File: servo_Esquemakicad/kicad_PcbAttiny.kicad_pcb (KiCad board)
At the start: 2 copper layers, 56 parts, among them J1 Conn_02x01, J10 Conn_01x04, J11 Conn_01x04, J12 Conn_01x04, J13 Conn_01x04, J2 Conn_02x02_Odd_Even, J3 Conn_02x02_Odd_Even, J4 Conn_01x04, J5 ESP01, J6 Conn_01x04, J7 Conn_01x04, J8 Conn_01x04, J9 Conn_01x04, K1 SANYOU_SRD_Form_C, K2 SANYOU_SRD_Form_C, K3 SANYOU_SRD_Form_C, K4 SANYOU_SRD_Form_C, K5 SANYOU_SRD_Form_C, K6 SANYOU_SRD_Form_C, K7 SANYOU_SRD_Form_C, K8 SANYOU_SRD_Form_C, Q1 2N2219, Q2 2N2219, Q3 2N2219, Q4 2N2219, Q5 2N2219, Q6 2N2219, Q7 2N2219, Q8 2N2219, U1 ATtiny85V-10PU, U2 74HC595, U3 L7809, U4 L7805, U5 LM317

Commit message: att
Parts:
- removed the C1 at (123.6, 56.5)
- removed C3: 220u, Capacitor_THT:CP_Radial_D5.0mm_P2.50mm
- removed J1: Conn_02x01, Connector_PinHeader_2.54mm:PinHeader_2x01_P2.54mm_Vertical
- removed the J2 at (127.6, 47.5)
- removed the J3 at (176.3, 47.5)
- removed the U3 at (140.6, 49.0)
- removed U4: L7805, Package_TO_SOT_THT:TO-220-3_Vertical
- C1: renamed from C4; value 47u -> 0.1u
- C2: value 47u -> 10u
- J2: renamed from J4; value Conn_01x04 -> RF
- moved R1 60.9 mm to (148.6, 53.3), turned to 180 degrees
- moved U2 55.3 mm to (138.4, 58.4), turned to 270 degrees
- moved U1 48.8 mm to (153.7, 114.3), turned to 90 degrees
- moved R8 41.4 mm to (118.1, 121.9), turned to 90 degrees
- moved R2 39.9 mm to (141.0, 69.8)
- moved C1 37.5 mm to (132.1, 57.1)
- moved U3 35.7 mm to (129.5, 114.3)
- moved R7 28.4 mm to (118.1, 100.3), turned to 90 degrees
- moved R9 20.6 mm to (171.4, 121.9), turned to 90 degrees
- moved R6 18.7 mm to (118.1, 80.0), turned to 90 degrees
- moved J3 16.1 mm to (141.0, 78.7)
- moved R5 16.0 mm to (118.1, 58.4), turned to 90 degrees
- moved J2 13.6 mm to (151.1, 76.2)
- moved C2 11.0 mm to (133.3, 67.3), turned to 90 degrees
- moved R12 8.34 mm to (171.4, 59.7), turned to 90 degrees
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- renumbered D5 to D1, D1 to D2, D6 to D3, D2 to D4, D7 to D5, D3 to D6, D8 to D7, D4 to D8, J13 to J10, J6 to J11, J5 to J3, J10 to J4, J9 to J5, J11 to J6, J8 to J7, J12 to J8, J7 to J9, K5 to K1, K1 to K2, K6 to K3, K2 to K4, K7 to K5, K3 to K6, K8 to K7, K4 to K8, Q5 to Q2, Q2 to Q3, Q6 to Q4, Q3 to Q5, Q7 to Q6, Q4 to Q7, R9 to R1, R3 to R10, R2 to R11, R1 to R12, R10 to R2, R8 to R5, R7 to R6, R6 to R7, R5 to R8, R4 to R9, U5 to U2, U2 to U3
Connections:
- C1 pad 2: GND -> Net-(C1-Pad2)
- C2 pad 1: Net-(C2-Pad1) -> /+3.3V
- C2 pad 2: GND -> Net-(C1-Pad2)
- J10 pad 3: Net-(J13-Pad3) -> (no net)
- J11 pad 3: Net-(J6-Pad3) -> (no net)
- J3 pad 3: Net-(J5-Pad3) -> (no net)
- J3 pad 5: Net-(J5-Pad5) -> (no net)
- J3 pad 6: Net-(J5-Pad6) -> (no net)
- J4 pad 3: Net-(J10-Pad3) -> (no net)
- J5 pad 3: Net-(J9-Pad3) -> (no net)
- J6 pad 3: Net-(J11-Pad3) -> (no net)
- J7 pad 3: Net-(J8-Pad3) -> (no net)
- J8 pad 3: Net-(J12-Pad3) -> (no net)
- J9 pad 3: Net-(J7-Pad3) -> (no net)
- Q1 pad 3: Net-(J3-Pad1) -> /+5V
- Q2 pad 3: Net-(J3-Pad1) -> /+5V
- Q3 pad 3: Net-(J3-Pad1) -> /+5V
- Q4 pad 3: Net-(J3-Pad1) -> /+5V
- Q5 pad 3: Net-(J3-Pad1) -> /+5V
- Q6 pad 3: Net-(J3-Pad1) -> /+5V
- Q7 pad 3: Net-(J3-Pad1) -> /+5V
- Q8 pad 3: Net-(J3-Pad1) -> /+5V
- R1 pad 2: GND -> Net-(C1-Pad2)
- U1 pad 8: Net-(U1-Pad8) -> (no net)
- U3 pad 9: Net-(U2-Pad9) -> (no net)
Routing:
- net GND: track 637.4 -> 255.0 mm
- net Net-(J3-Pad1): track 295.8 -> 0.00 mm, vias 6 -> 0
- net /RX: track 117.4 -> 0.00 mm, vias 4 -> 0
- net /+3.3V: track 84.6 -> 0.00 mm
- net Net-(C1-Pad1): track 82.6 -> 0.00 mm, vias 8 -> 0
- net +12V: track 74.8 -> 0.00 mm, vias 4 -> 0
- net /TX: track 69.6 -> 0.00 mm
- net /EN: track 59.4 -> 0.00 mm, vias 4 -> 0
- net /Q4: track 41.3 -> 0.00 mm
- net Net-(C1-Pad1) (its old number): track 40.9 -> 0.00 mm
- net Net-(C2-Pad1): track 38.6 -> 0.00 mm
- net Net-(R11-Pad1): track 35.1 -> 0.00 mm
- net Net-(R12-Pad1): track 30.4 -> 0.00 mm
- net Net-(R9-Pad1): track 30.0 -> 0.00 mm
- net /Q3: track 26.8 -> 0.00 mm
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- removed copper zone on B.Cu, net (none)
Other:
- board text removed: "+12V"
- board text removed: "+5V"
- board text removed: "7805"
- board text removed: "7809"
- board text removed: "Alim"
- board text removed: "Alim."
- board text removed: "GND"
- board text removed: "J4"
- board text removed: "J5"
- board text removed: "Jumper"

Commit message: retirada de componentes desnecessarios
após analise vi q vários componentes n tinham razão pra existir então foram retirado
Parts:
- removed D1, D2, D3, D4, D5, D6, D7, D8: 1N4007, Diode_THT:D_DO-41_SOD81_P10.16mm_Horizontal
- removed J10, J11, J4, J5, J6, J7, J8, J9: Conn_01x04, TerminalBlock:TerminalBlock_bornier-4_P5.08mm
- removed K1, K2, K3, K4, K5, K6, K7, K8: SANYOU_SRD_Form_C, Relay_THT:Relay_SPDT_SANYOU_SRD_Series_Form_C
- removed U1: ATtiny85V-10PU, Package_DIP:DIP-8_W7.62mm_Socket
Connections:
- Q1 pad 1: /K1 -> (no net)
- Q1 pad 3: /+5V -> (no net)
- Q2 pad 1: /K5 -> (no net)
- Q2 pad 3: /+5V -> (no net)
- Q3 pad 1: /K2 -> (no net)
- Q3 pad 3: /+5V -> (no net)
- Q4 pad 1: /K6 -> (no net)
- Q4 pad 3: /+5V -> (no net)
- Q5 pad 1: /K3 -> (no net)
- Q5 pad 3: /+5V -> (no net)
- Q6 pad 1: /K7 -> (no net)
- Q6 pad 3: /+5V -> (no net)
- Q7 pad 1: /K4 -> (no net)
- Q7 pad 3: /+5V -> (no net)
- Q8 pad 1: /K8 -> (no net)
- Q8 pad 3: /+5V -> (no net)
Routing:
- net GND: track 255.0 -> 0.00 mm
- net /+5V: track 78.0 -> 0.00 mm, vias 6 -> 0
- net Net-(J8-Pad4): track 29.2 -> 0.00 mm
- net Net-(J6-Pad4): track 29.2 -> 0.00 mm
- net Net-(J4-Pad4): track 29.2 -> 0.00 mm
- net Net-(J10-Pad4): track 29.2 -> 0.00 mm
- net Net-(J9-Pad4): track 28.3 -> 0.00 mm
- net Net-(J7-Pad4): track 28.3 -> 0.00 mm
- net Net-(J11-Pad4): track 28.3 -> 0.00 mm
- net Net-(J5-Pad4): track 28.3 -> 0.00 mm
- net /K7: track 19.1 -> 0.00 mm
- net /K6: track 19.1 -> 0.00 mm
- net /K5: track 19.1 -> 0.00 mm
- net /K8: track 19.1 -> 0.00 mm
- net /K4: track 19.0 -> 0.00 mm
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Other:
- board text removed: "COM"
- board text removed: "NC"
- board text removed: "NF"
- board text removed: "NO"

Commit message: atualizações do esquematico e design PCB
Atualizada o esquemático com as novas conexões p/ os transistores
Atualizado o designe PCB com os novos footprints
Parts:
- removed C1: 0.1u, Capacitor_THT:CP_Radial_D5.0mm_P2.50mm
- removed C2: 10u, Capacitor_THT:CP_Radial_D5.0mm_P2.50mm
- removed R1: 220R, Resistor_THT:R_Axial_DIN0207_L6.3mm_D2.5mm_P10.16mm_Horizontal
- removed R2: 360R, Resistor_THT:R_Axial_DIN0207_L6.3mm_D2.5mm_P10.16mm_Horizontal
- removed U2: LM317, Package_TO_SOT_THT:TO-220-3_Horizontal_TabDown
- added J1: Jack-DC, Connector_BarrelJack:BarrelJack_Horizontal, F.Cu at (226.3, 50.6)
- added R3: 2k, Resistor_THT:R_Axial_DIN0207_L6.3mm_D2.5mm_P10.16mm_Horizontal, F.Cu at (213.3, 59.9)
- added R4: 1k, Resistor_THT:R_Axial_DIN0207_L6.3mm_D2.5mm_P10.16mm_Horizontal, F.Cu at (230.4, 47.2)
- added U1: ATtiny85, Package_SO:SOIJ-8_5.3x5.3mm_P1.27mm, F.Cu at (197.5, 50.2)

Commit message: init design PCB
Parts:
- removed U1: ATtiny85, Package_SO:SOIJ-8_5.3x5.3mm_P1.27mm
- added U2: ATtiny85-20PU, Package_DIP:DIP-8_W7.62mm, F.Cu at (167.6, 57.1)
- moved J1 111.6 mm to (115.6, 64.8), turned to 270 degrees
- moved R4 94.6 mm to (135.9, 52.1), turned to 180 degrees
- moved R3 60.2 mm to (153.7, 52.1), turned to 180 degrees
- moved R8 53.2 mm to (141.4, 74.0), turned to 270 degrees
- moved R9 51.9 mm to (151.4, 74.0), turned to 270 degrees
- moved U3 49.8 mm to (124.5, 64.8)
- moved Q7 42.4 mm to (142.7, 89.0), turned to 180 degrees
- moved J3 40.6 mm to (179.1, 64.8), turned to 180 degrees
- moved Q8 37.1 mm to (182.7, 89.0), turned to 180 degrees
- moved Q2 36.6 mm to (152.7, 89.0), turned to 180 degrees
- moved Q1 34.2 mm to (112.7, 89.0), turned to 180 degrees
- moved R7 29.5 mm to (131.4, 74.0), turned to 270 degrees
- moved R10 29.3 mm to (161.4, 74.0), turned to 270 degrees
- moved J2 27.3 mm to (163.8, 52.1)
- moved Q5 22.5 mm to (132.7, 89.0), turned to 180 degrees
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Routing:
- net /+5V: track 0.00 -> 115.5 mm
- net /TX: track 0.00 -> 69.9 mm
- net Net-(R12-Pad1): track 0.00 -> 46.3 mm
- net Net-(R11-Pad1): track 0.00 -> 41.3 mm
- net Net-(U2-Pad6): track 0.00 -> 39.0 mm
- net Net-(U2-Pad7): track 0.00 -> 34.7 mm
- net Net-(R10-Pad1): track 0.00 -> 33.8 mm
- net GND: track 0.00 -> 30.0 mm
- net Net-(R5-Pad1): track 0.00 -> 29.3 mm
- net Net-(R9-Pad1): track 0.00 -> 26.2 mm
- net Net-(U2-Pad5): track 0.00 -> 26.0 mm
- net Net-(R8-Pad1): track 0.00 -> 19.4 mm
- net /RX: track 0.00 -> 13.0 mm
- net Net-(R6-Pad1): track 0.00 -> 11.3 mm
- net Net-(R7-Pad1): track 0.00 -> 10.9 mm
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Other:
- board text removed: "ATtiny85"
- board text removed: "LM317"

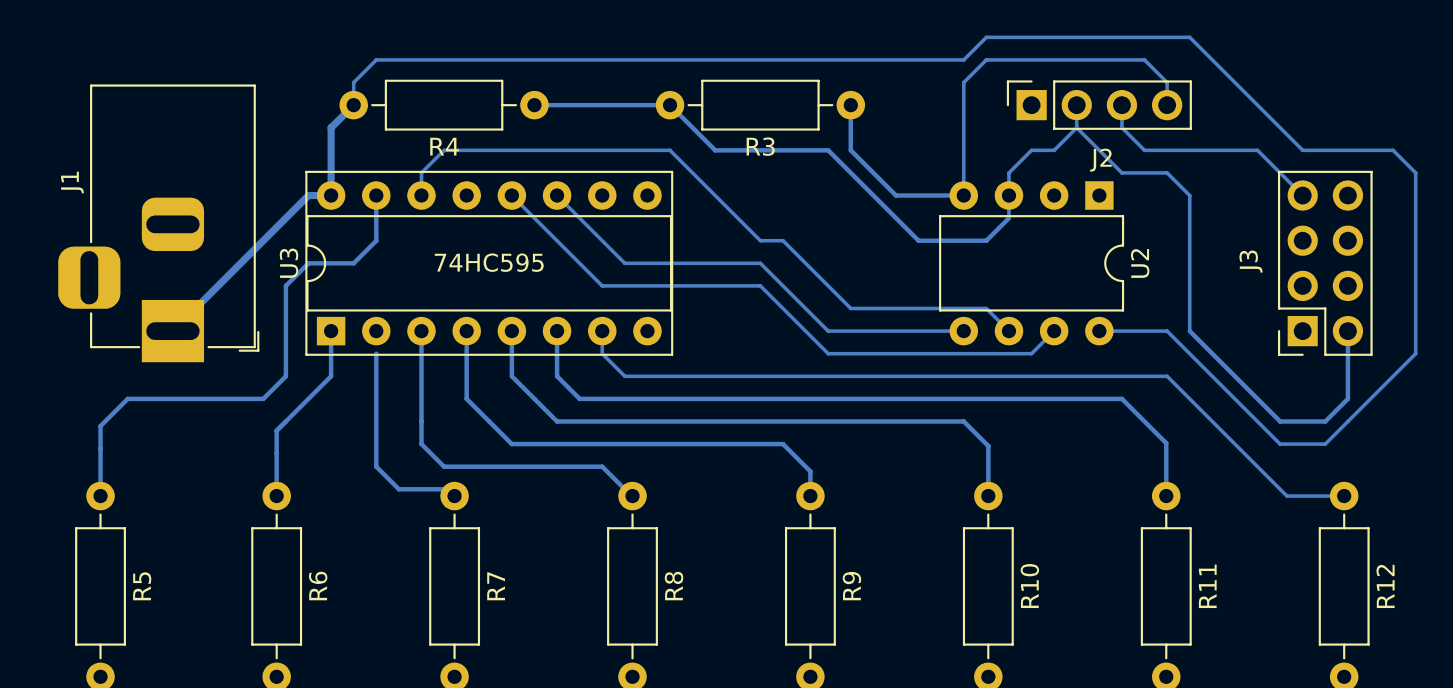
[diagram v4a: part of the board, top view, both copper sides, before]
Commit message: trilhas terminadas
Falta as vias para as saídas dos transistores.
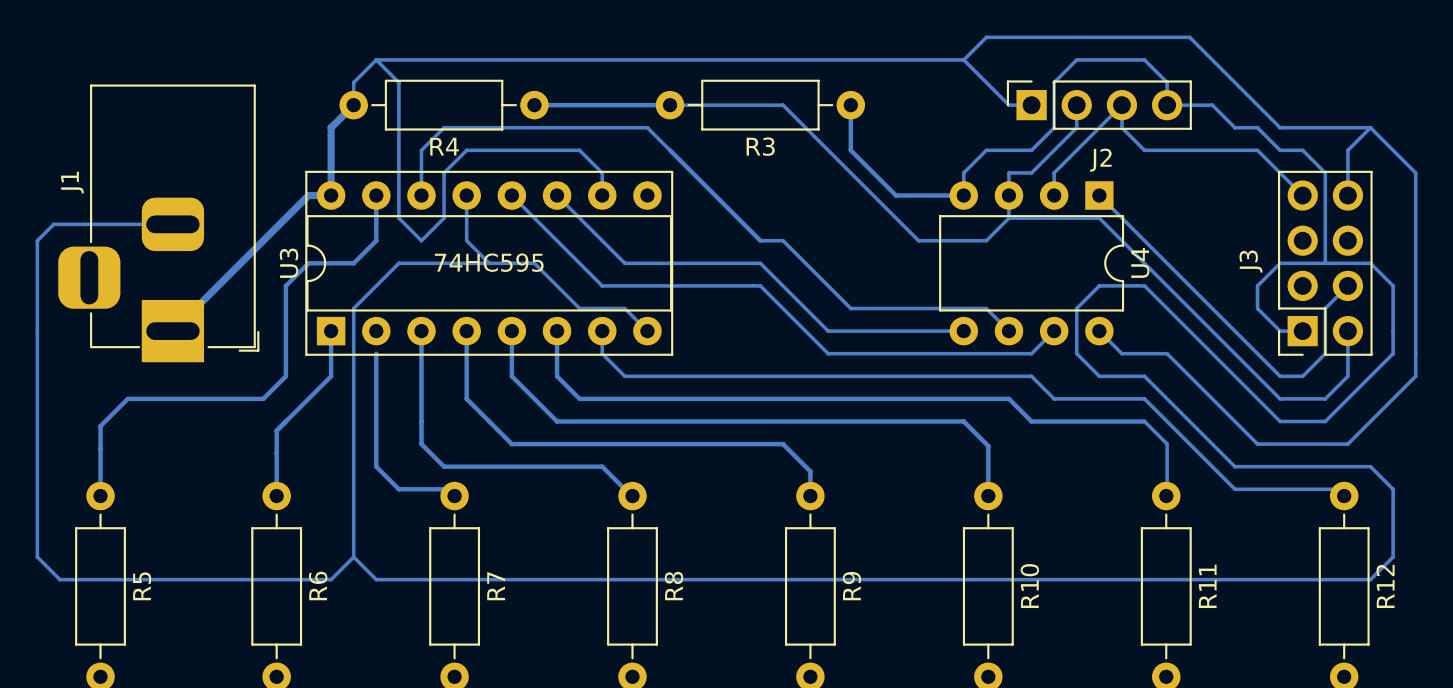
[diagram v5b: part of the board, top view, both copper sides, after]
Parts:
- removed U2: ATtiny85-20PU, Package_DIP:DIP-8_W7.62mm
- added U4: ATtiny85-20PU, Package_DIP:DIP-8_W7.62mm, F.Cu at (167.6, 57.1)
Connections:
- J2 pad 1: /+3.3V -> /+5V
- J3 pad 8: /+3.3V -> /+5V
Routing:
- net GND: track 30.0 -> 252.8 mm
- net /+5V: track 115.5 -> 152.2 mm
- net /EN: track 0.00 -> 21.8 mm
- net /RX: track 13.0 -> 19.7 mm
- net /TX: track 69.9 -> 65.3 mm
- net Net-(U3-Pad14): track 39.0 -> 40.8 mm
